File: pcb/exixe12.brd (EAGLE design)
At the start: 20 x 40 mm, 43 parts

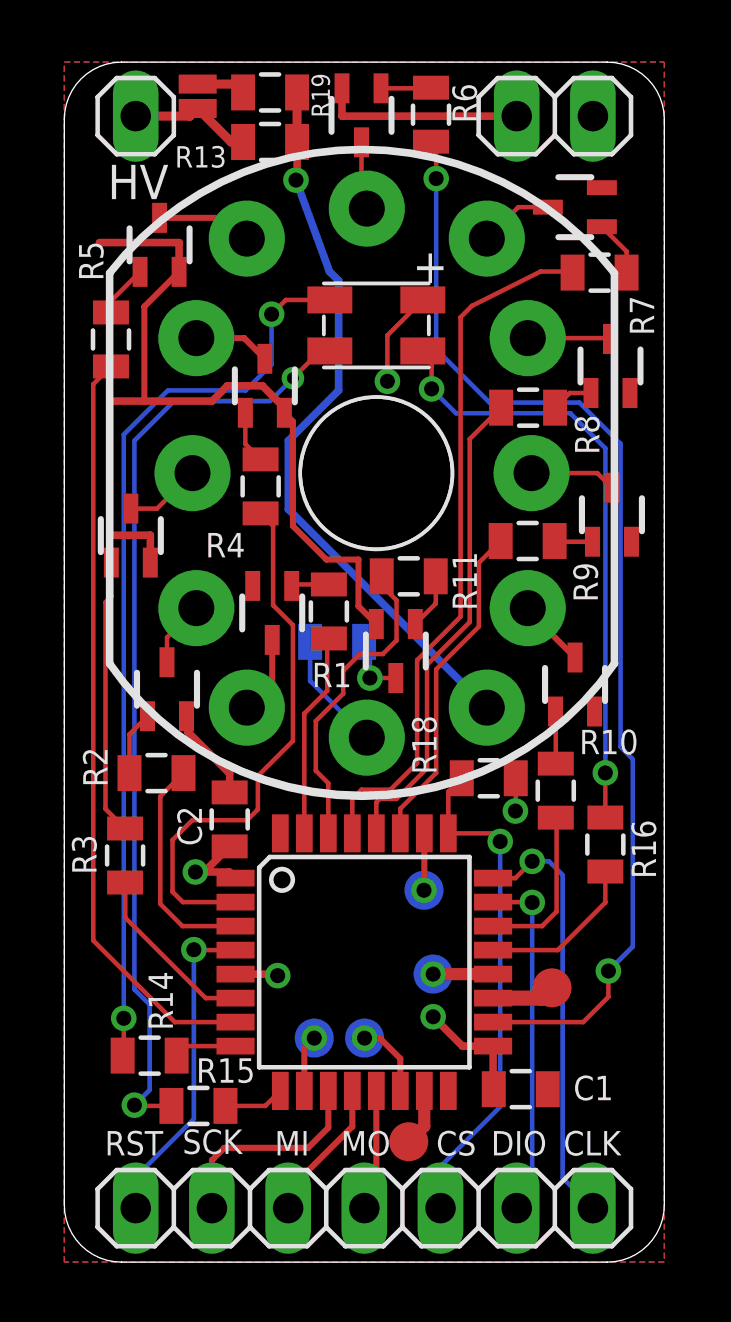
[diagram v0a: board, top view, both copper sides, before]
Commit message: adjusted resistor
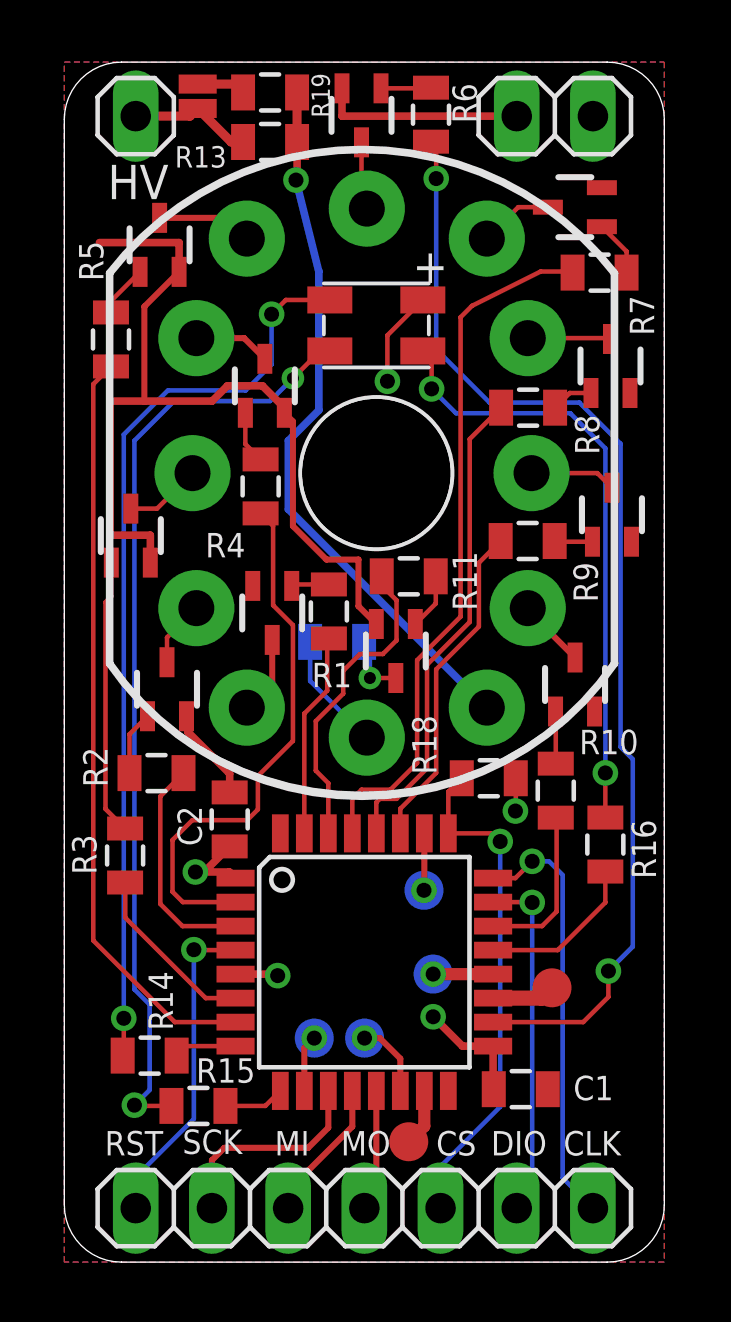
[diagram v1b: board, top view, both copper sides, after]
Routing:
- net +180V: track 24.3 -> 23.8 mm
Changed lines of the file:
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@@
 <polygon width="0.254" layer="42">
 <vertex x="7.366" y="36.0172"/>
-<vertex x="8.5344" y="32.5628"/>
-<vertex x="8.7884" y="29.21"/>
+<vertex x="8.0264" y="33.02"/>
+<vertex x="8.0264" y="28.6004"/>
 <vertex x="7.1628" y="27.4828"/>
 <vertex x="7.1628" y="24.892"/>
@@
 <vertex x="13.4112" y="19.812"/>
 <vertex x="8.0264" y="25.2984"/>
-<vertex x="9.5504" y="29.1592"/>
-<vertex x="9.398" y="33.0708"/>
-<vertex x="8.0264" y="36.6268"/>
+<vertex x="8.89" y="28.1432"/>
+<vertex x="8.89" y="33.1216"/>
+<vertex x="7.9248" y="36.4744"/>
 <vertex x="7.2644" y="36.3728"/>
 <vertex x="7.366" y="36.068"/>
@@
 <wire x1="7.758" y1="38.989" x2="7.758" y2="37.338" width="0.3048" layer="1"/>
 <via x="7.7216" y="36.068" extent="1-16" drill="0.5"/>
-<wire x1="8.8392" y1="33.02" x2="7.7216" y2="36.068" width="0.254" layer="16"/>
+<wire x1="7.7216" y1="36.068" x2="8.4836" y2="33.02" width="0.254" layer="16"/>
 <wire x1="7.758" y1="37.338" x2="7.758" y2="36.1044" width="0.254" layer="1"/>
 <wire x1="7.758" y1="36.1044" x2="7.7216" y2="36.068" width="0.254" layer="1"/>
 <wire x1="7.4676" y1="25.0974" x2="14.0825" y2="18.4825" width="0.254" layer="16"/>
-<wire x1="7.4676" y1="25.0974" x2="7.4676" y2="27.3812" width="0.254" layer="16"/>
-<wire x1="9.144" y1="32.7152" x2="8.8392" y2="33.02" width="0.254" layer="16"/>
-<wire x1="7.4676" y1="27.3812" x2="9.144" y2="29.0576" width="0.254" layer="16"/>
-<wire x1="9.144" y1="29.0576" x2="9.144" y2="32.7152" width="0.254" layer="16"/>
+<wire x1="7.4676" y1="27.3812" x2="7.4676" y2="25.0974" width="0.254" layer="16"/>
+<wire x1="8.4836" y1="33.02" x2="8.4836" y2="28.3972" width="0.254" layer="16"/>
+<wire x1="8.4836" y1="28.3972" x2="7.4676" y2="27.3812" width="0.254" layer="16"/>
 </signal>
 <signal name="GND">
@@
 <wire x1="10.7696" y1="30.8926" x2="11.95" y2="32.073" width="0.1524" layer="1"/>
 <via x="15.0368" y="15.0368" extent="1-16" drill="0.5"/>
-<wire x1="15.0876" y1="16.2416" x2="15.0478" y2="16.129" width="0.1524" layer="1"/>
 <wire x1="15.0478" y1="16.129" x2="15.0478" y2="15.0478" width="0.1524" layer="1"/>
 <wire x1="15.0478" y1="15.0478" x2="15.0368" y2="15.0368" width="0.1524" layer="1"/>
@@
 <signal name="STM_1">
 <contactref element="R1" pad="1"/>
-<wire x1="8.763" y1="19.05" x2="8.763" y2="20.633" width="0.1524" layer="1"/>
-<wire x1="8.763" y1="20.633" x2="8.818" y2="20.7896" width="0.1524" layer="1"/>
 <contactref element="U$2" pad="31"/>
 <wire x1="8" y1="14.2926" x2="8" y2="18.287" width="0.1524" layer="1"/>
 <wire x1="8" y1="18.287" x2="8.763" y2="19.05" width="0.1524" layer="1"/>
+<wire x1="8.763" y1="19.05" x2="8.763" y2="20.7346" width="0.1524" layer="1"/>
+<wire x1="8.763" y1="20.7346" x2="8.818" y2="20.7896" width="0.1524" layer="1"/>
 </signal>
 <signal name="N$21">
@@
 <contactref element="Q11" pad="3"/>
 <contactref element="R12" pad="1"/>
-<via x="10.1854" y="19.4708" extent="1-16" drill="0.5"/>
+<via x="10.1854" y="19.4708" extent="1-16" drill="0.4"/>
 <wire x1="11.049" y1="19.4708" x2="10.1854" y2="19.4708" width="0.1524" layer="1"/>
 <wire x1="9.9932" y1="20.6756" x2="10.1854" y2="20.6756" width="0.1524" layer="16"/>

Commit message: ready to fab
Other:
- board text added: "RX"
- board text added: "TX"
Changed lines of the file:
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@@
 <text x="10.414" y="14.224" size="1.27" layer="26" font="vector" rot="MR0">exixe12</text>
 <text x="10.414" y="11.176" size="1.27" layer="26" font="vector" rot="MR0">dekuNukem</text>
+<text x="15.4432" y="7.2644" size="1.016" layer="25" font="vector">TX</text>
+<text x="11.3284" y="9.0932" size="1.016" layer="26" font="vector" rot="MR0">RX</text>
 </plain>
 <attributes>
@@
 <wire x1="9.6" y1="15.442" x2="9.906" y2="15.748" width="0.1524" layer="1"/>
 <wire x1="11.7602" y1="16.637" x2="11.7602" y2="20.066" width="0.1524" layer="1"/>
-<wire x1="13.208" y1="31.496" x2="13.589" y2="31.877" width="0.1524" layer="1"/>
-<wire x1="13.589" y1="31.877" x2="15.875" y2="33.02" width="0.1524" layer="1"/>
+<wire x1="15.875" y1="33.02" x2="13.589" y2="31.877" width="0.1524" layer="1"/>
 <wire x1="15.875" y1="33.02" x2="16.906" y2="33.02" width="0.1524" layer="1"/>
 <wire x1="16.906" y1="33.02" x2="16.942" y2="32.984" width="0.1524" layer="1"/>
 <wire x1="9.906" y1="15.748" x2="10.8712" y2="15.748" width="0.1524" layer="1"/>
 <wire x1="10.8712" y1="15.748" x2="11.7602" y2="16.637" width="0.1524" layer="1"/>
-<wire x1="11.7602" y1="20.066" x2="13.208" y2="21.5138" width="0.1524" layer="1"/>
-<wire x1="13.208" y1="21.5138" x2="13.208" y2="31.496" width="0.1524" layer="1"/>
+<wire x1="13.208" y1="21.5138" x2="11.7602" y2="20.066" width="0.1524" layer="1"/>
+<wire x1="13.589" y1="31.877" x2="13.589" y2="28.1178" width="0.1524" layer="1"/>
+<wire x1="13.589" y1="28.1178" x2="13.208" y2="27.7368" width="0.1524" layer="1"/>
+<wire x1="13.208" y1="27.7368" x2="13.208" y2="21.5138" width="0.1524" layer="1"/>
 </signal>
 <signal name="STM_8">

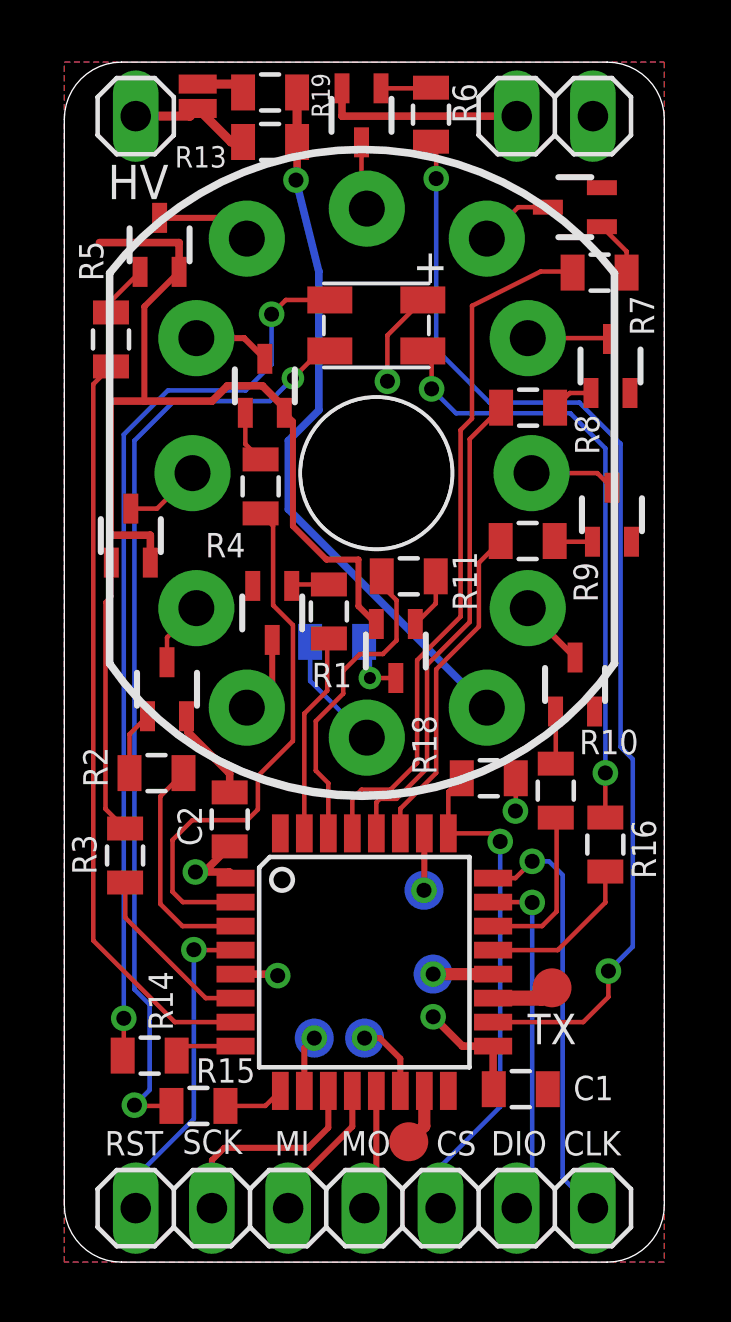
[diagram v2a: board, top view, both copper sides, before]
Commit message: added pulldown on boot0
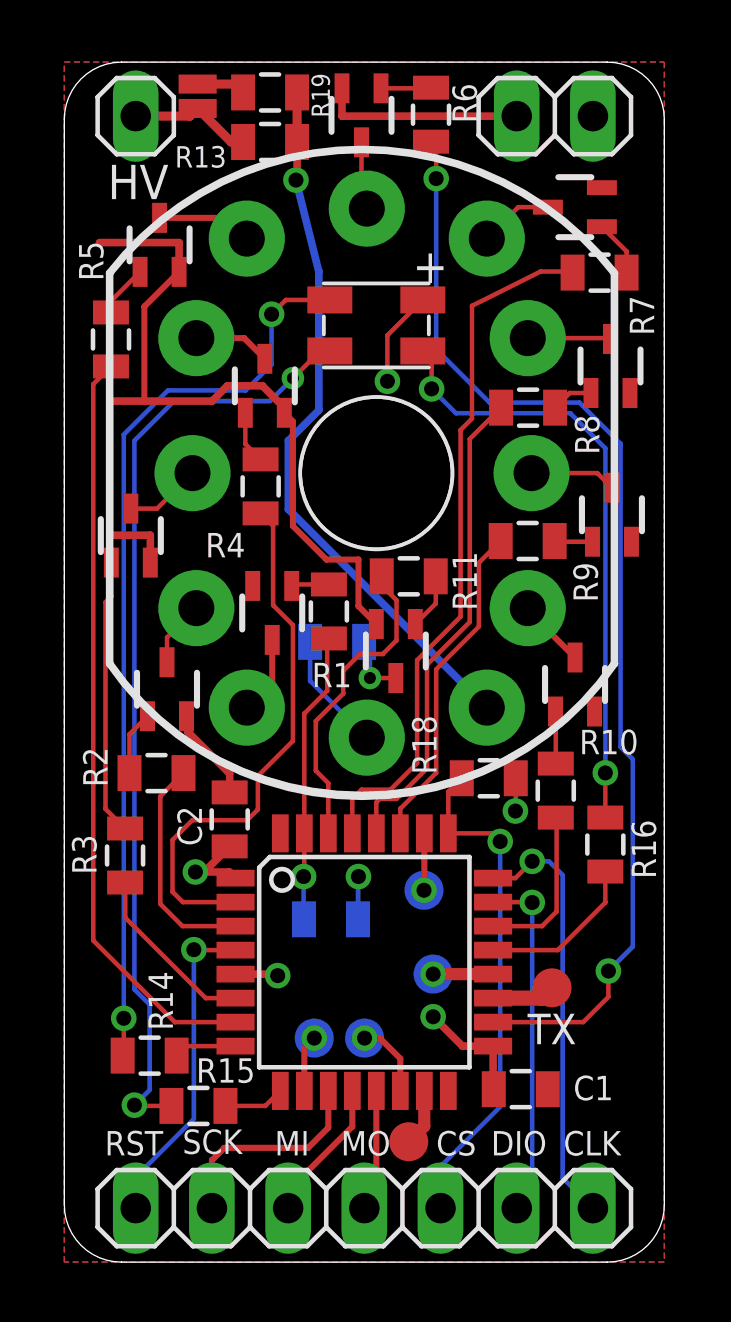
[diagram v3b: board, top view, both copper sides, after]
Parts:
- added R17: 47K, joyAnalog:0805
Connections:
- net GND: now also R17.1
- net STM_1: now also R17.2
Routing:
- net STM_1: track 6.84 -> 9.71 mm, vias 0 -> 1
- net GND: track 40.5 -> 41.9 mm, vias 0 -> 1
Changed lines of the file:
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@@
 <attribute name="VALUE" x="10.1092" y="19.2786" size="0.4064" layer="28" rot="MR0"/>
+</element>
+<element name="R17" library="joyAnalog" package="0805" value="47K" x="8.89" y="11.43" smashed="yes" rot="MR0">
+<attribute name="NAME" x="12.5476" y="10.7823" size="0.8128" layer="26" rot="MR0"/>
 </element>
 </elements>
@@
 <wire x1="8.7376" y1="23.4188" x2="9.8044" y2="23.4188" width="0.2032" layer="1"/>
 <wire x1="9.8044" y1="23.4188" x2="9.8044" y2="21.8654" width="0.2032" layer="1"/>
+<contactref element="R17" pad="1"/>
+<via x="9.8044" y="12.8524" extent="1-16" drill="0.5"/>
+<wire x1="9.79" y1="11.43" x2="9.79" y2="12.838" width="0.1524" layer="16"/>
+<wire x1="9.79" y1="12.838" x2="9.8044" y2="12.8524" width="0.1524" layer="16"/>
 </signal>
 <signal name="N$1">
@@
 <contactref element="R1" pad="1"/>
 <contactref element="U$2" pad="31"/>
-<wire x1="8" y1="14.2926" x2="8" y2="18.287" width="0.1524" layer="1"/>
+<wire x1="8" y1="18.287" x2="8" y2="14.2926" width="0.1524" layer="1"/>
 <wire x1="8" y1="18.287" x2="8.763" y2="19.05" width="0.1524" layer="1"/>
 <wire x1="8.763" y1="19.05" x2="8.763" y2="20.7346" width="0.1524" layer="1"/>
 <wire x1="8.763" y1="20.7346" x2="8.818" y2="20.7896" width="0.1524" layer="1"/>
+<contactref element="R17" pad="2"/>
+<via x="7.9756" y="12.8524" extent="1-16" drill="0.5"/>
+<wire x1="7.9756" y1="12.8524" x2="7.9756" y2="11.9524" width="0.1524" layer="16"/>
+<wire x1="7.9756" y1="11.9524" x2="7.99" y2="11.43" width="0.1524" layer="16"/>
+<wire x1="8" y1="14.2926" x2="8" y2="12.8768" width="0.1524" layer="1"/>
+<wire x1="8" y1="12.8768" x2="7.9756" y2="12.8524" width="0.1524" layer="1"/>
 </signal>
 <signal name="N$21">

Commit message: updated to use timer
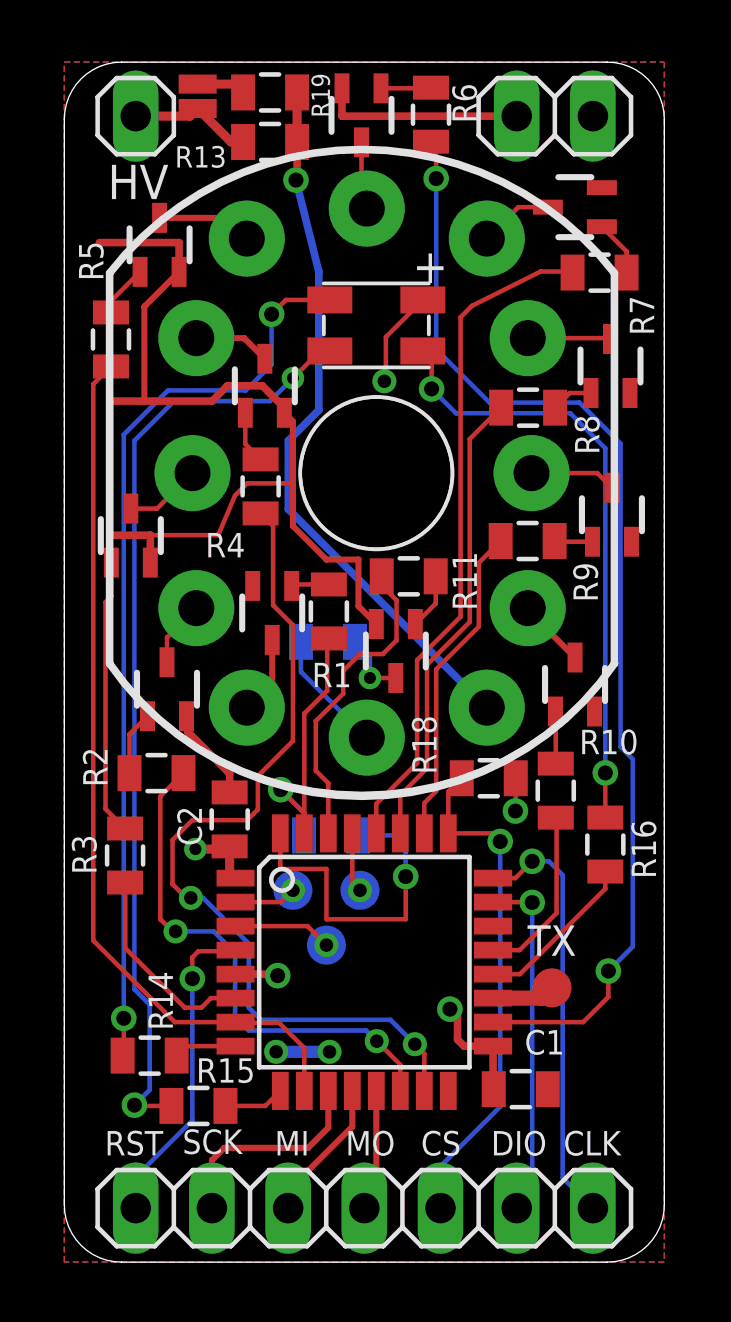
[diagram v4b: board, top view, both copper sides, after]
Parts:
- removed TP4, TP6: PTR1TP13R, nixx:TP13R
- R1, R10, R11, R18, R2, R3, R4, R5, R6, R7, R8, R9: value 4K7 -> 10K
- R12: value 47K -> 510K
- R15: value 470 -> 1K
- R16: value 0 -> 470
- moved TP3 5.48 mm to (7.62, 12.4)
- moved TP5 3.73 mm to (8.74, 10.6)
- moved TP2 3.71 mm to (9.86, 12.4)
- moved R17 2.79 mm to (8.89, 14.2)
- moved R12 0.30 mm to (8.79, 20.7)
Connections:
- removed net N$18: TP4.TP, U$2.15
- removed net N$20: TP5.TP, U$2.26
- net N$14: now also TP2.TP, U$2.29; no longer TP6.TP, U$2.10
- net N$16: now also TP3.TP, U$2.2; no longer TP2.TP, U$2.20
- net N$17: now also TP5.TP, U$2.3; no longer TP3.TP, U$2.14
- net PWM_BLUE: now also U$2.20; no longer U$2.21
- net STM_10: now also U$2.21; no longer U$2.22
- net STM_2: now also U$2.14; no longer U$2.3
- net STM_4: now also U$2.15; no longer U$2.2
- net STM_5: now also U$2.10
- net STM_7: now also U$2.28; no longer U$2.29
- net STM_8: now also U$2.27; no longer U$2.28
- net STM_9: now also U$2.26; no longer U$2.27
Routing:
- net GND: track 41.9 -> 59.2 mm, vias 1 -> 3
- net STM_4: track 18.0 -> 28.8 mm, vias 0 -> 2
- net STM_2: track 7.49 -> 17.3 mm, vias 0 -> 2
- net STM_5: track 25.2 -> 29.3 mm
- net N$18: track 1.91 -> 0.00 mm
- net N$20: track 1.90 -> 0.00 mm, vias 1 -> 0
- net STM_7: track 23.4 -> 22.5 mm
- net STM_3: track 5.96 -> 6.82 mm
- net STM_1: track 9.71 -> 10.5 mm
- net N$17: track 2.55 -> 3.29 mm
- net STM_8: track 16.2 -> 15.6 mm
- net +3V3: track 12.5 -> 11.9 mm
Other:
- board text added: "dekuNukem 2017"
- board text removed: "RX"
- board text removed: "dekuNukem"
